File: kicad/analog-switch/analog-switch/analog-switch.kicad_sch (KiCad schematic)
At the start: 12 parts, among them J1 Conn_01x04, J2 Conn_01x16_MountingPin, J3 Conn_02x01_Row_Letter_First, J4 Conn_01x04, J5 Conn_01x16_MountingPin, Q1 Q_PNP_EBC, U1 CD74HC4067M, U2 74HC595, U3 CD74HC4067M

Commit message: proj settings
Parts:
- removed J1, J4: Conn_01x04, Connector_PinHeader_2.54mm:PinHeader_1x04_P2.54mm_Vertical, symbol Connector_Generic:Conn_01x04
- removed J2, J5: Conn_01x16_MountingPin, Connector_PinHeader_2.54mm:PinHeader_1x16_P2.54mm_Vertical, symbol Connector_Generic_MountingPin:Conn_01x16_MountingPin
- removed J3: Conn_02x01_Row_Letter_First, symbol Connector_Generic:Conn_02x01_Row_Letter_First
- added J1: Conn_01x05_Male, Connector_PinHeader_2.00mm:PinHeader_1x05_P2.00mm_Vertical, symbol Connector:Conn_01x05_Male
- added J2, J5: Conn_01x17_Male, Connector_PinHeader_2.54mm:PinHeader_1x17_P2.54mm_Vertical, symbol Connector:Conn_01x17_Male
- added J4: Conn_01x03_Female, Connector_PinHeader_2.00mm:PinHeader_1x03_P2.00mm_Vertical, symbol Connector:Conn_01x03_Female
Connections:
- net +5V: now also J5.17 (Pin_17)
- net GND: now also R3.1, J2.17 (Pin_17); no longer R3.2
- net at U2.9 (QH'): now also J4.1 (Pin_1)
- net at U2.12 (RCLK): now also J4.2 (Pin_2)
- net at R1.2, U2.13 (~{OE}): now also R2.2, J1.5 (Pin_5), J4.3 (Pin_3); no longer R2.1
- net AN2: now reaches U3.1 (COM)
- net AN2: now also J1.2 (Pin_2)
- net at Q1.3 (C), U1.15 (~{E}), U3.15 (~{E}): now also R3.2; no longer R3.1
- net at U3.16 (I15): now also J5.16 (Pin_16)
- net at U3.17 (I14): now also J5.15 (Pin_15)
- net at U3.18 (I13): now also J5.14 (Pin_14)
- net at U3.19 (I12): now also J5.13 (Pin_13)
- net at U3.2 (I7): now also J5.8 (Pin_8)
- net at U3.20 (I11): now also J5.12 (Pin_12)
- net at U3.21 (I10): now also J5.11 (Pin_11)
- net at U3.22 (I9): now also J5.10 (Pin_10)
- net at U3.23 (I8): now also J5.9 (Pin_9)
- net at U3.3 (I6): now also J5.7 (Pin_7)
- net at U3.4 (I5): now also J5.6 (Pin_6)
- net at U3.5 (I4): now also J5.5 (Pin_5)
- net at U3.6 (I3): now also J5.4 (Pin_4)
- net at U3.7 (I2): now also J5.3 (Pin_3)
- net at U3.8 (I1): now also J5.2 (Pin_2)
- net at U3.9 (I0): now also J5.1 (Pin_1)
- net AN1: now reaches U1.1 (COM)
- net AN1: now also J1.1 (Pin_1)
- net at U1.16 (I15): now also J2.16 (Pin_16)
- net at U1.17 (I14): now also J2.15 (Pin_15)
- net at U1.18 (I13): now also J2.14 (Pin_14)
- net at U1.19 (I12): now also J2.13 (Pin_13)
- net at U1.2 (I7): now also J2.8 (Pin_8)
- net at U1.20 (I11): now also J2.12 (Pin_12)
- net at U1.21 (I10): now also J2.11 (Pin_11)
- net at U1.22 (I9): now also J2.10 (Pin_10)
- net at U1.23 (I8): now also J2.9 (Pin_9)
- net at U1.3 (I6): now also J2.7 (Pin_7)
- net at U1.4 (I5): now also J2.6 (Pin_6)
- net at U1.5 (I4): now also J2.5 (Pin_5)
- net at U1.6 (I3): now also J2.4 (Pin_4)
- net at U1.7 (I2): now also J2.3 (Pin_3)
- net at U1.8 (I1): now also J2.2 (Pin_2)
- net at U1.9 (I0): now also J2.1 (Pin_1)
- net at U2.11 (SRCLK): now also J1.4 (Pin_4)
- net at U2.14 (SER): now also J1.3 (Pin_3)
- net at Q1.2 (B): now also R2.1; no longer R2.2
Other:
- moved on the sheet: Q1, R1, R2, R3, U1, U2, U3

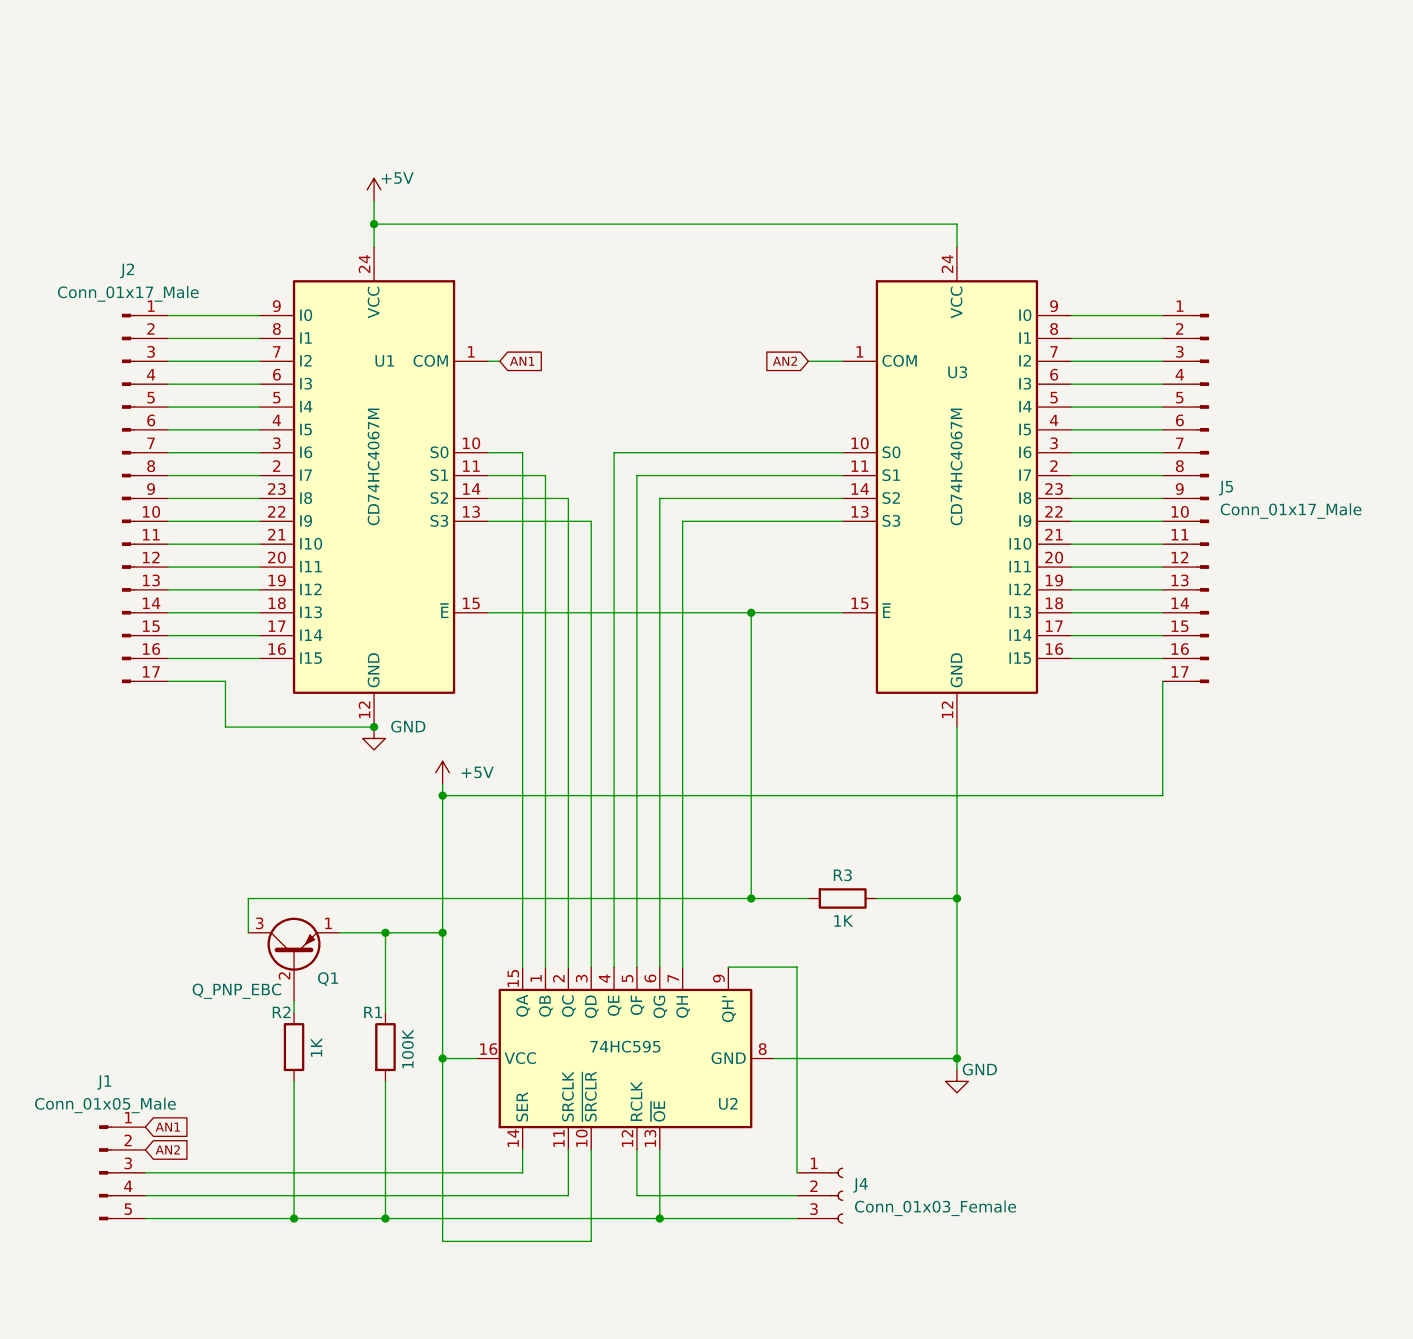
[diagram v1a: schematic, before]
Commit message: make analog-sw to DIP-40
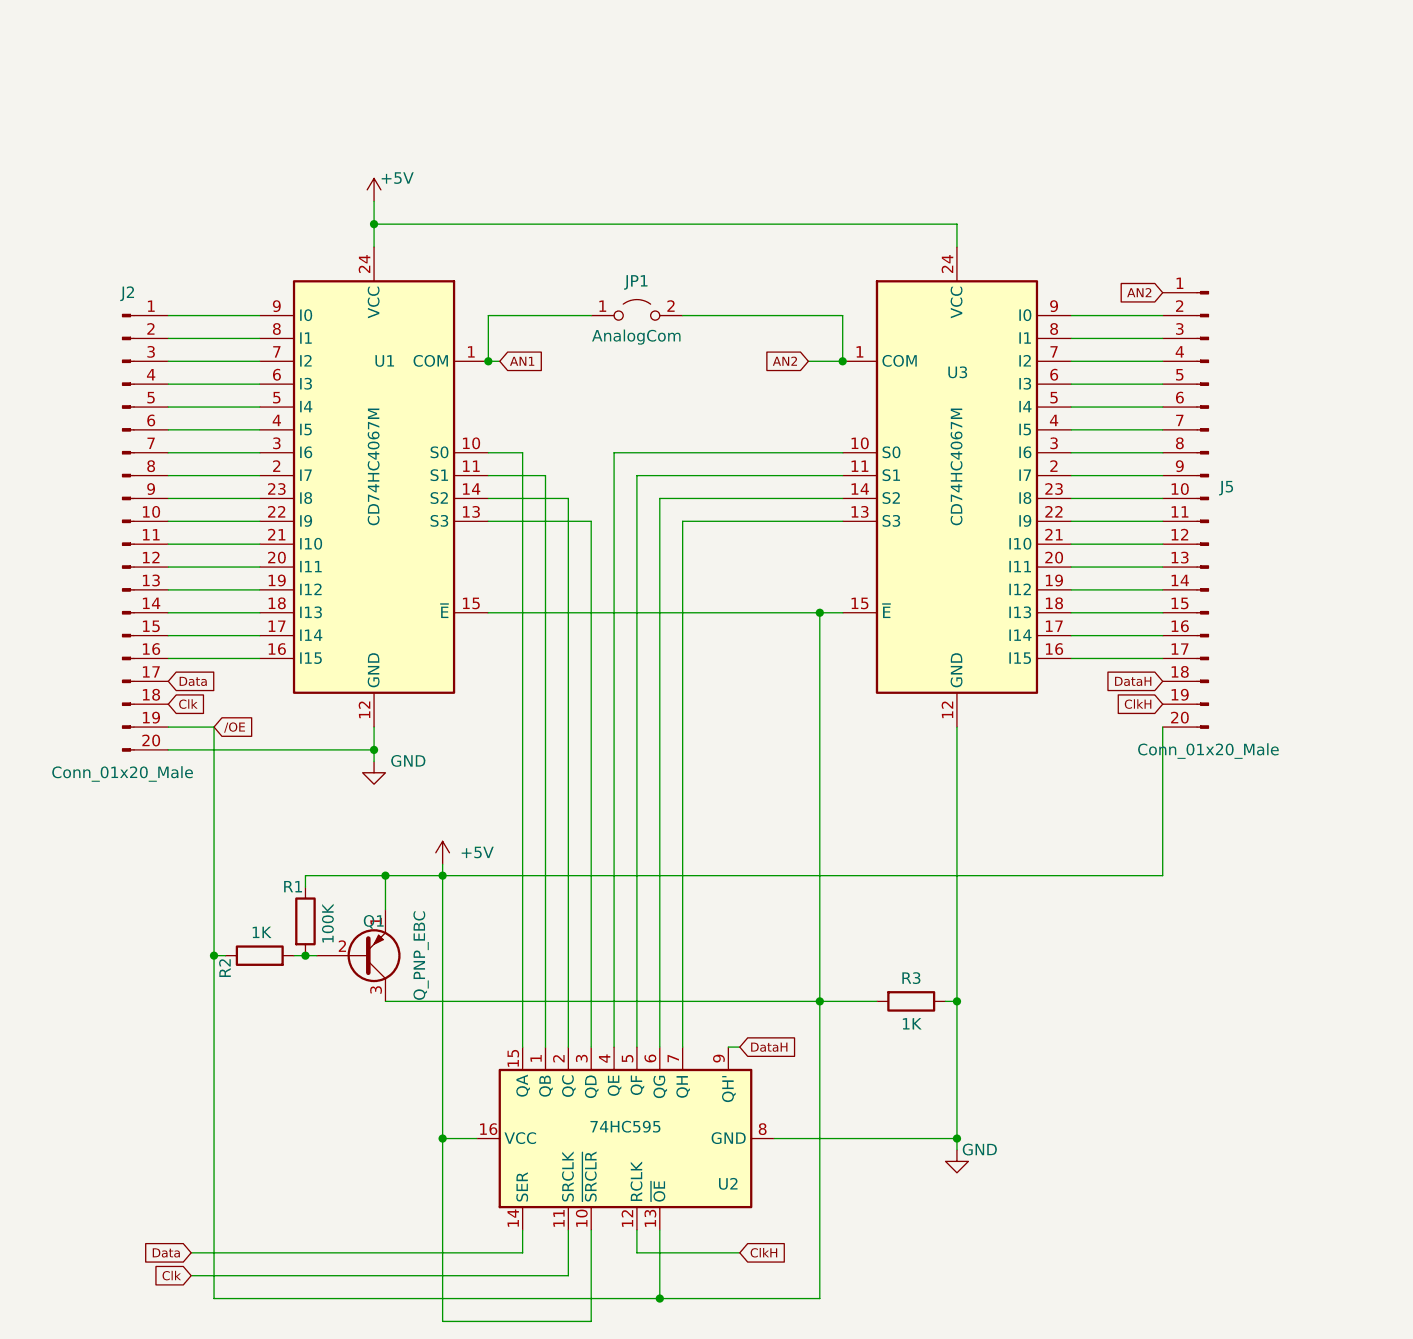
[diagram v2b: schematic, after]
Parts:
- removed J1: Conn_01x05_Male, Connector_PinHeader_2.00mm:PinHeader_1x05_P2.00mm_Vertical, symbol Connector:Conn_01x05_Male
- removed J4: Conn_01x03_Female, Connector_PinHeader_2.00mm:PinHeader_1x03_P2.00mm_Vertical, symbol Connector:Conn_01x03_Female
- added JP1: AnalogCom, Connector_PinHeader_2.54mm:PinHeader_1x02_P2.54mm_Vertical, symbol Jumper:Jumper_2_Open
- J2, J5: value Conn_01x17_Male -> Conn_01x20_Male; footprint Connector_PinHeader_2.54mm:PinHeader_1x17_P2.54mm_Vertical -> Connector_PinHeader_2.54mm:PinHeader_1x20_P2.54mm_Vertical; symbol Connector:Conn_01x17_Male -> Connector:Conn_01x20_Male
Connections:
- net +5V: now also J5.20 (Pin_20); no longer J5.17 (Pin_17)
- net AN1: now also JP1.1 (A)
- net AN2: now also J5.1 (Pin_1), JP1.2 (B)
- net GND: now also J2.20 (Pin_20); no longer J2.17 (Pin_17)
- net /OE: now reaches Q1.3 (C), R3.2, U1.15 (~{E}), U3.15 (~{E})
- net /OE: now also J2.19 (Pin_19), R2.1, U2.13 (~{OE})
- net at U3.16 (I15): now also J5.17 (Pin_17); no longer J5.16 (Pin_16)
- net at U3.17 (I14): now also J5.16 (Pin_16); no longer J5.15 (Pin_15)
- net at U3.18 (I13): now also J5.15 (Pin_15); no longer J5.14 (Pin_14)
- net at U3.19 (I12): now also J5.14 (Pin_14); no longer J5.13 (Pin_13)
- net at U3.2 (I7): now also J5.9 (Pin_9); no longer J5.8 (Pin_8)
- net at U3.20 (I11): now also J5.13 (Pin_13); no longer J5.12 (Pin_12)
- net at U3.21 (I10): now also J5.12 (Pin_12); no longer J5.11 (Pin_11)
- net at U3.22 (I9): now also J5.11 (Pin_11); no longer J5.10 (Pin_10)
- net at U3.23 (I8): now also J5.10 (Pin_10); no longer J5.9 (Pin_9)
- net at U3.3 (I6): now also J5.8 (Pin_8); no longer J5.7 (Pin_7)
- net at U3.4 (I5): now also J5.7 (Pin_7); no longer J5.6 (Pin_6)
- net at U3.5 (I4): now also J5.6 (Pin_6); no longer J5.5 (Pin_5)
- net at U3.6 (I3): now also J5.5 (Pin_5); no longer J5.4 (Pin_4)
- net at U3.7 (I2): now also J5.4 (Pin_4); no longer J5.3 (Pin_3)
- net at U3.8 (I1): now also J5.3 (Pin_3); no longer J5.2 (Pin_2)
- net at U3.9 (I0): now also J5.2 (Pin_2); no longer J5.1 (Pin_1)
- net Data: now reaches U2.14 (SER)
- net Data: now also J2.17 (Pin_17)
- net Clk: now reaches U2.11 (SRCLK)
- net Clk: now also J2.18 (Pin_18)
- net at R1.2, R2.2: now also Q1.2 (B); no longer U2.13 (~{OE})
- net ClkH: now reaches U2.12 (RCLK)
- net ClkH: now also J5.19 (Pin_19)
- net DataH: now reaches U2.9 (QH')
- net DataH: now also J5.18 (Pin_18)
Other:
- moved on the sheet: Q1, R1, R2, R3, U2
